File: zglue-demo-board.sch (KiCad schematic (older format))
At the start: 142 parts, among them J1 20021121-00010C4LF, J10 0473460001, J2 DF13A-2P-1.25H, J3 20021121-00010C4LF, J4 2x20_Header_Female, J5 0473460001, J6 556500488, J7 556500488, J8 WE_686115148922, J9 WE_686115148922_FLIPPED, U1 MCP1700T-3302E_TT, U2 NTB0104BQ, U3 NTB0104BQ, U4 NTB0104BQ, U5 93LC56CT-IMC, U6 FT4232HQ, U7 NTB0104BQ, U8 NTB0104BQ, Y1 ASFLMB-12.000MHZ-LC-T

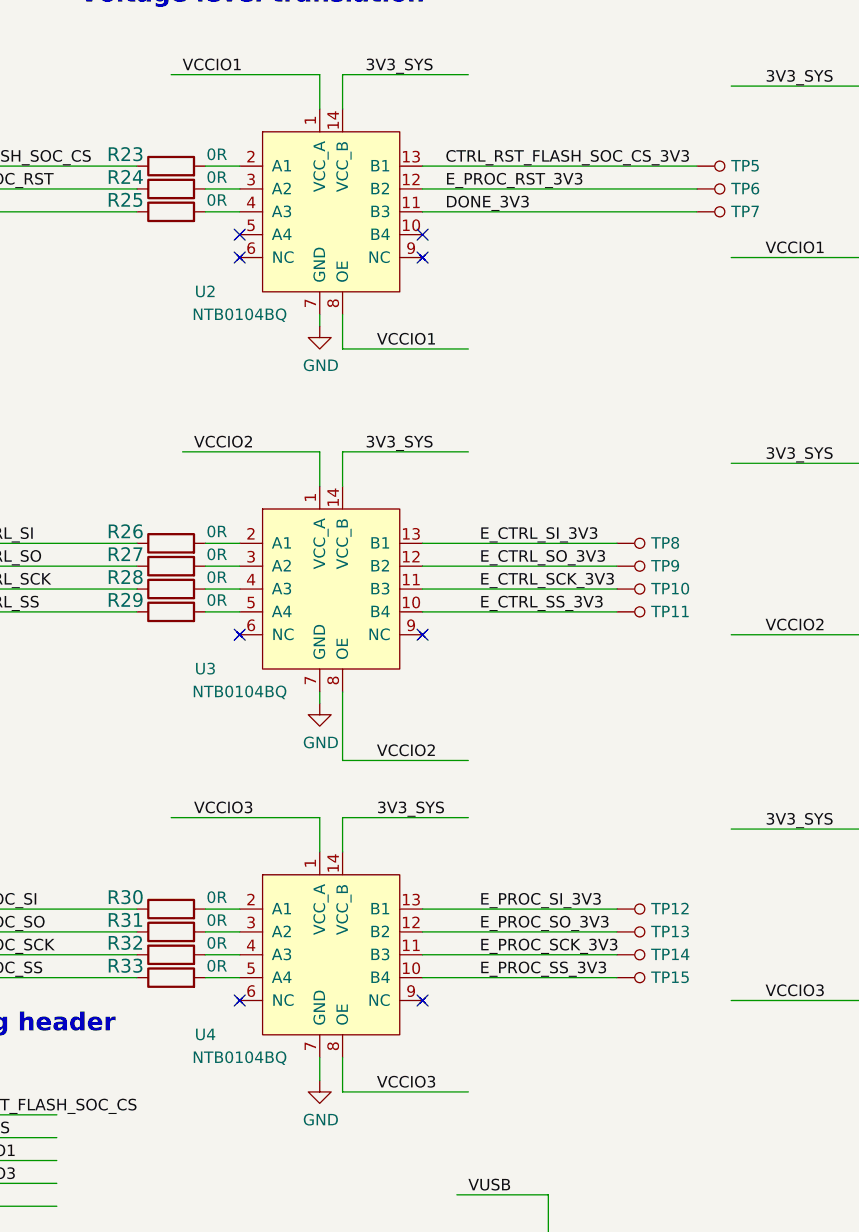
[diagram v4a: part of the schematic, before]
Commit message: Schematic updated after initial bringup
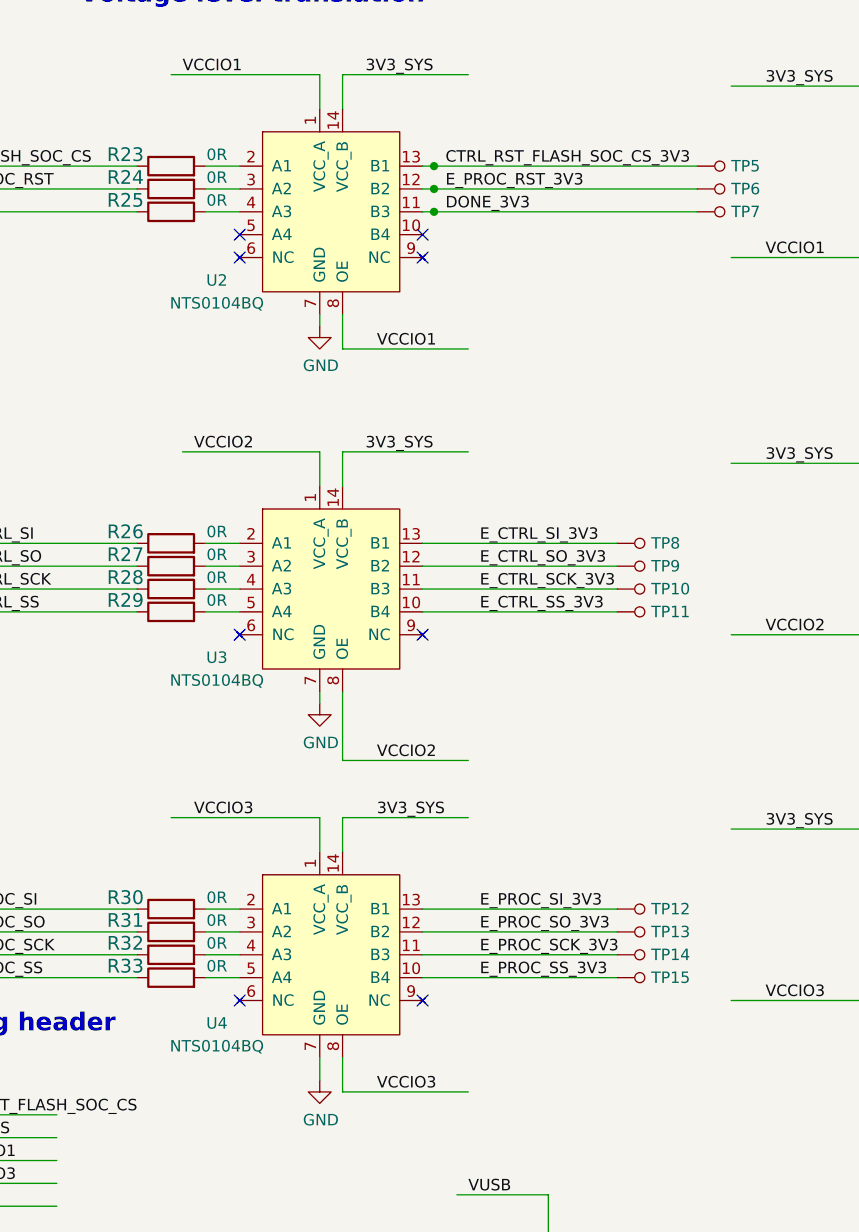
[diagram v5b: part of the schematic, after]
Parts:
- removed U2, U3, U4: NTB0104BQ, antmicro-footprints:QDHVQFN14, symbol antmicroLogicTranslatorsLevelShifters:NTB0104BQ
- added U2, U3, U4: NTS0104BQ, antmicro-footprints:QDHVQFN14, symbol antmicroLogicTranslatorsLevelShifters:NTS0104BQ
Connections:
- wire segments 516 -> 519
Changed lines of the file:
@@
 EESchema Schematic File Version 4
 LIBS:zglue-demo-board-cache
-EELAYER 26 0
+EELAYER 30 0
 EELAYER END
 $Descr A3 16535 11693
@@
 TODO: check pin order\n
 $Comp
-L antmicroLogicTranslatorsLevelShifters:NTB0104BQ U4
-U 1 1 5D99B71D
-P 6800 5000
-F 0 "U4" H 6250 4650 50  0000 C CNN
-F 1 "NTB0104BQ" H 6400 4550 50  0000 C CNN
-F 2 "antmicro-footprints:QDHVQFN14" H 7850 5650 50  0001 C CNN
-F 3 "https://datasheet.octopart.com/NTB0104BQ%2C115-NXP-Semiconductors-datasheet-12519051.pdf" H 7450 5750 50  0001 C CNN
-F 4 "NTB0104BQ" H 6800 5536 50  0001 C CNN "MPN"
-F 5 "NXP Semiconductors" H 6800 5537 50  0001 C CNN "Manufacturer"
-	1    6800 5000
-	1    0    0    -1
-$EndComp
-$Comp
 L power:GND #PWR026
 U 1 1 5D9BD547
@@
 $EndComp
 $Comp
-L antmicroLogicTranslatorsLevelShifters:NTB0104BQ U3
-U 1 1 5DC43970
-P 6800 3400
-F 0 "U3" H 6250 3050 50  0000 C CNN
-F 1 "NTB0104BQ" H 6400 2950 50  0000 C CNN
-F 2 "antmicro-footprints:QDHVQFN14" H 7850 4050 50  0001 C CNN
-F 3 "https://datasheet.octopart.com/NTB0104BQ%2C115-NXP-Semiconductors-datasheet-12519051.pdf" H 7450 4150 50  0001 C CNN
-F 4 "NTB0104BQ" H 6800 3936 50  0001 C CNN "MPN"
-F 5 "NXP Semiconductors" H 6800 3937 50  0001 C CNN "Manufacturer"
-	1    6800 3400
-	1    0    0    -1
-$EndComp
-$Comp
 L power:GND #PWR025
 U 1 1 5DC43977
@@
 E_CTRL_SS_3V3
 $Comp
-L antmicroLogicTranslatorsLevelShifters:NTB0104BQ U2
-U 1 1 5DD333E1
-P 6800 1750
-F 0 "U2" H 6250 1400 50  0000 C CNN
-F 1 "NTB0104BQ" H 6400 1300 50  0000 C CNN
-F 2 "antmicro-footprints:QDHVQFN14" H 7850 2400 50  0001 C CNN
-F 3 "https://datasheet.octopart.com/NTB0104BQ%2C115-NXP-Semiconductors-datasheet-12519051.pdf" H 7450 2500 50  0001 C CNN
-F 4 "NTB0104BQ" H 6800 2286 50  0001 C CNN "MPN"
-F 5 "NXP Semiconductors" H 6800 2287 50  0001 C CNN "Manufacturer"
-	1    6800 1750
-	1    0    0    -1
-$EndComp
-$Comp
 L power:GND #PWR024
 U 1 1 5DD333E8
@@
 	5950 1750 4850 1750
 Wire Wire Line
-	8400 1550 7200 1550
+	8400 1550 7250 1550
 Wire Wire Line
-	8400 1750 7200 1750
+	8400 1750 7250 1750
 $Comp
 L antmicroTestPoints:TP_SMD1MM TP5
@@
 NoConn ~ 7200 5200
 Wire Wire Line
-	8400 1650 7200 1650
+	8400 1650 7250 1650
 Text Label 5150 1650 0    50   ~ 0
 E_PROC_RST
@@
 Wire Wire Line
 	11400 3950 10750 3950
+$Comp
+L antmicroLogicTranslatorsLevelShifters:NTS0104BQ U2
+U 1 1 5DE18FC3
+P 6800 1750
+F 0 "U2" H 6300 1450 50  0000 C CNN
+F 1 "NTS0104BQ" H 6300 1350 50  0000 C CNN
+F 2 "antmicro-footprints:QDHVQFN14" H 7850 2400 50  0001 C CNN
+F 3 "https://datasheet.octopart.com/NTS0104BQ%2C115-NXP-Semiconductors-datasheet-11805065.pdf" H 7450 2500 50  0001 C CNN
+F 4 "NTS0104BQ" H 6800 2289 50  0001 C CNN "MPN"
+F 5 "NXP Semiconductors" H 6800 2290 50  0001 C CNN "Manufacturer"
+	1    6800 1750
+	1    0    0    -1
+$EndComp
+Connection ~ 7250 1750
+Wire Wire Line
+	7250 1750 7200 1750
+Connection ~ 7250 1650
+Wire Wire Line
+	7250 1650 7200 1650
+Connection ~ 7250 1550
+Wire Wire Line
+	7250 1550 7200 1550
+$Comp
+L antmicroLogicTranslatorsLevelShifters:NTS0104BQ U3
+U 1 1 5DE1ADF0
+P 6800 3400
+F 0 "U3" H 6300 3100 50  0000 C CNN
+F 1 "NTS0104BQ" H 6300 3000 50  0000 C CNN
+F 2 "antmicro-footprints:QDHVQFN14" H 7850 4050 50  0001 C CNN
+F 3 "https://datasheet.octopart.com/NTS0104BQ%2C115-NXP-Semiconductors-datasheet-11805065.pdf" H 7450 4150 50  0001 C CNN
+F 4 "NTS0104BQ" H 6800 3939 50  0001 C CNN "MPN"
+F 5 "NXP Semiconductors" H 6800 3940 50  0001 C CNN "Manufacturer"
+	1    6800 3400
+	1    0    0    -1
+$EndComp
+$Comp
+L antmicroLogicTranslatorsLevelShifters:NTS0104BQ U4
+U 1 1 5DE1BA96
+P 6800 5000
+F 0 "U4" H 6300 4700 50  0000 C CNN
+F 1 "NTS0104BQ" H 6300 4600 50  0000 C CNN
+F 2 "antmicro-footprints:QDHVQFN14" H 7850 5650 50  0001 C CNN
+F 3 "https://datasheet.octopart.com/NTS0104BQ%2C115-NXP-Semiconductors-datasheet-11805065.pdf" H 7450 5750 50  0001 C CNN
+F 4 "NTS0104BQ" H 6800 5539 50  0001 C CNN "MPN"
+F 5 "NXP Semiconductors" H 6800 5540 50  0001 C CNN "Manufacturer"
+	1    6800 5000
+	1    0    0    -1
+$EndComp
 $EndSCHEMATC

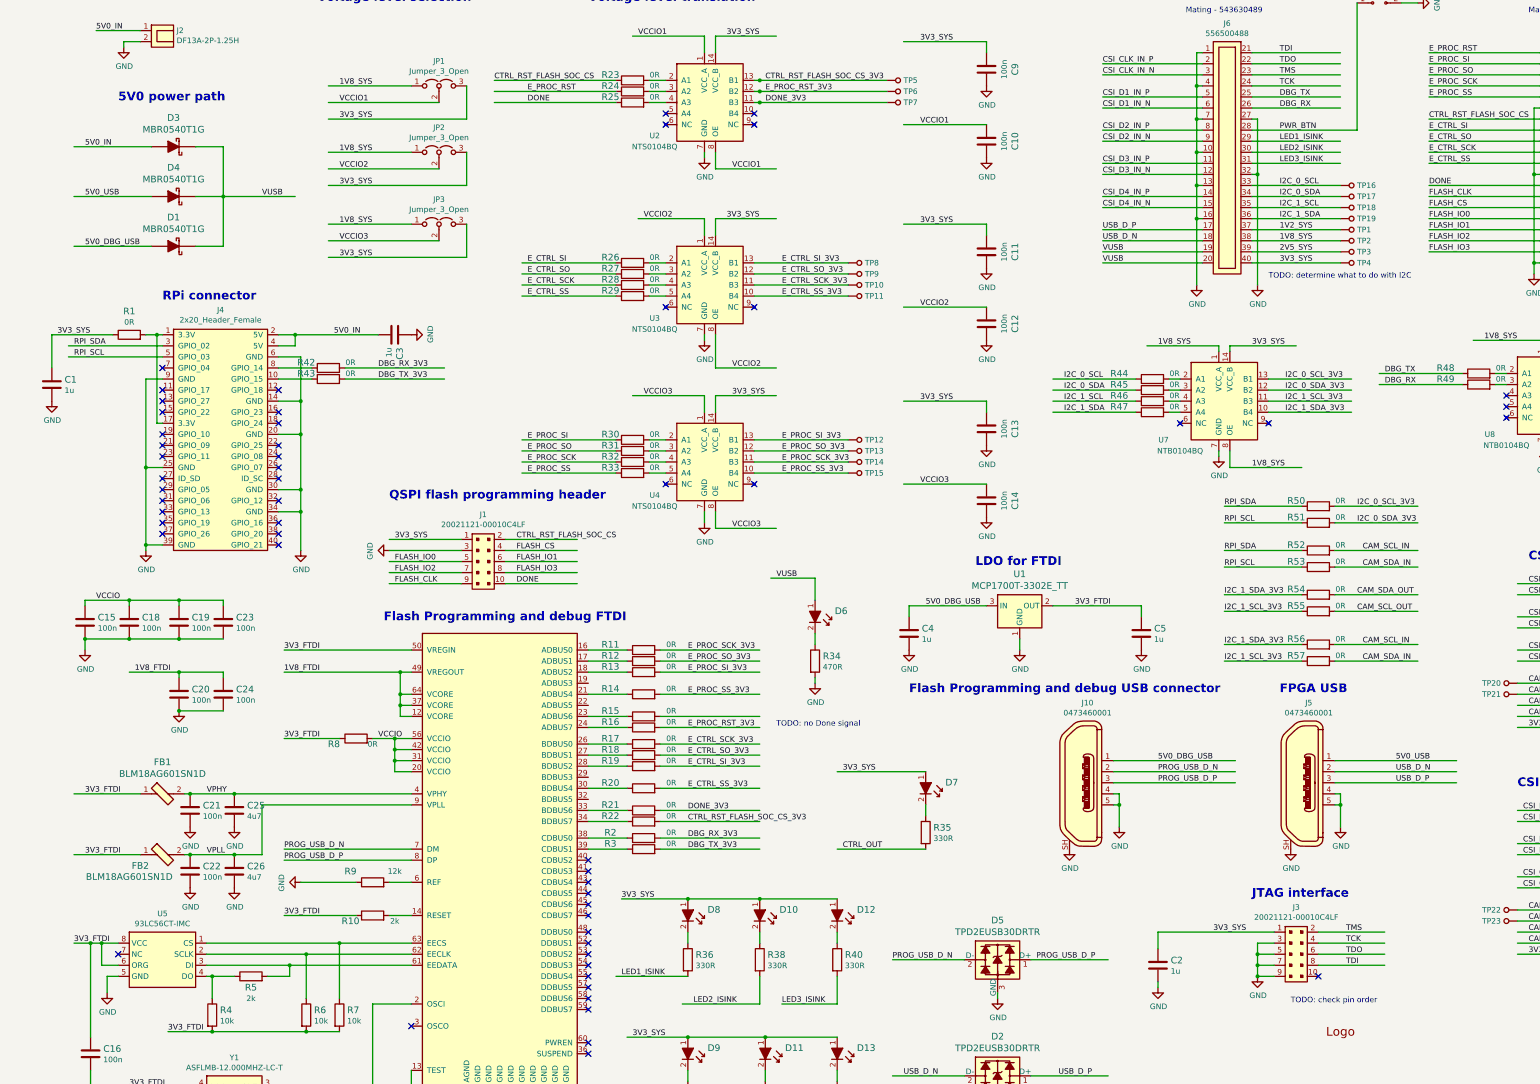
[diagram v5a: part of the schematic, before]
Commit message: Started revision 1.1, moved components to bottom side
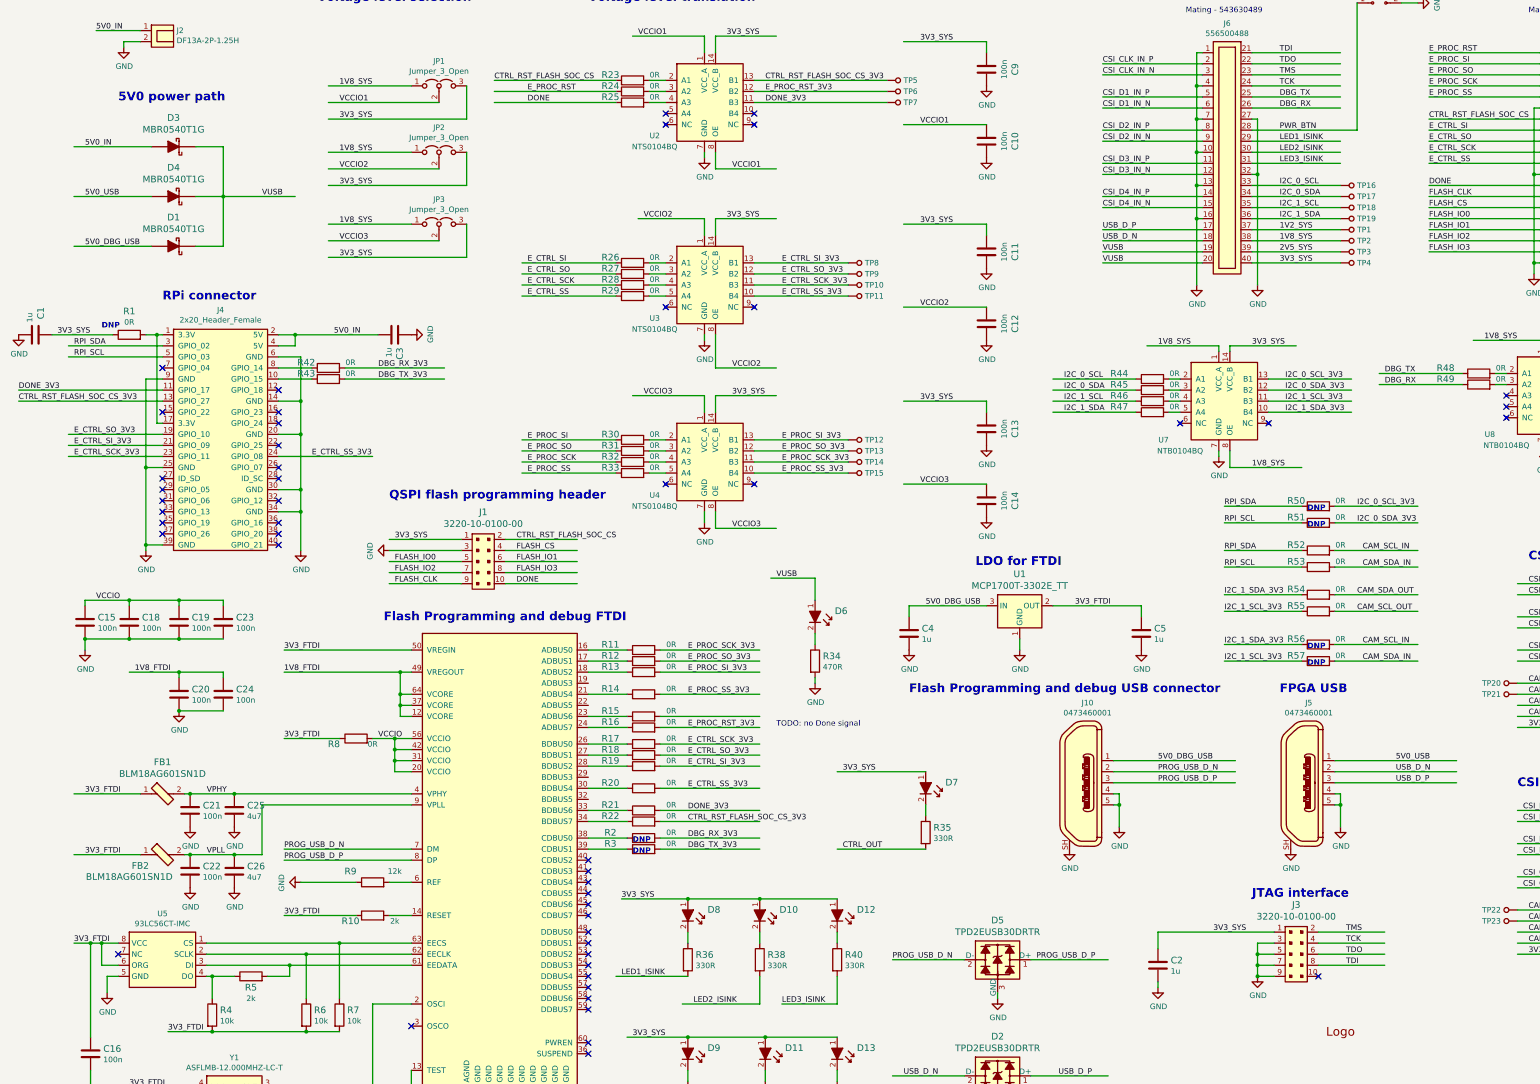
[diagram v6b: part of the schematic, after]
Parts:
- removed J1, J3: 20021121-00010C4LF, antmicro-footprints:PinHeader_2x5_P1.27mm, symbol antmicroRectangularConnectorsHeadersMalePins:20021121-00010C4LF
- added J1, J3: 3220-10-0100-00, antmicro-footprints:PinHeader_2x5_P1.27mm_Drill.7mm, symbol antmicroRectangularConnectorsHeadersMalePins:3220-10-0100-00
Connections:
- wire segments 519 -> 521
- no-connect marks 59 -> 53
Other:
- note added: "DNP"
- note removed: "TODO: check pin order\n"
- note removed: "TODO: determine what to do with I2C"
- moved on the sheet: C1
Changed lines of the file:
@@
 Title "zGlue Demo Board"
 Date ""
-Rev "1.0"
+Rev "1.1"
 Comp "Antmicro"
 Comment1 "www.antmicro.com"
@@
 Wire Wire Line
 	1650 1200 1500 1200
-$Comp
-L antmicroRectangularConnectorsHeadersMalePins:20021121-00010C4LF J3
-U 1 1 5DA5DFAD
-P 12100 9450
-F 0 "J3" H 12100 9875 50  0000 C CNN
-F 1 "20021121-00010C4LF" H 12100 9784 50  0000 C CNN
-F 2 "antmicro-footprints:PinHeader_2x5_P1.27mm" H 12300 9650 60  0001 L CNN
-F 3 "https://cdn.amphenol-icc.com/media/wysiwyg/files/drawing/20021121.pdf" H 12300 9750 60  0001 L CNN
-F 4 "20021121-00010C4LF" H 12300 9950 60  0001 L CNN "MPN"
-F 5 "Amphenol ICC (FCI)" H 12300 10550 60  0001 L CNN "Manufacturer"
-	1    12100 9450
-	1    0    0    -1
-$EndComp
 Wire Wire Line
 	11900 9250 10850 9250
@@
 L antmicroCapacitors0603:C_1u_0603 C1
 U 1 1 5DAD330C
-P 850 4300
-F 0 "C1" H 965 4345 60  0000 L CNN
-F 1 "C_1u_0603" H 850 4150 60  0001 C CNN
-F 2 "antmicro-footprints:0603-cap" H 1050 4500 60  0001 L CNN
-F 3 "" H 850 4300 50  0001 C CNN
-F 4 "WALSIN" H 1050 4700 60  0001 L CNN "Manufacturer"
-F 5 "0603X105K160CT" H 1050 4600 60  0001 L CNN "MPN"
-F 6 "1u" H 965 4247 50  0000 L CNN "Val"
-	1    850  4300
-	1    0    0    -1
+P 700 3850
+F 0 "C1" H 450 3900 60  0000 L CNN
+F 1 "C_1u_0603" H 700 3700 60  0001 C CNN
+F 2 "antmicro-footprints:0603-cap" H 900 4050 60  0001 L CNN
+F 3 "" H 700 3850 50  0001 C CNN
+F 4 "WALSIN" H 900 4250 60  0001 L CNN "Manufacturer"
+F 5 "0603X105K160CT" H 900 4150 60  0001 L CNN "MPN"
+F 6 "1u" H 500 3800 50  0000 L CNN "Val"
+	1    700  3850
+	0    1    1    0
 $EndComp
 $Comp
@@
 	1    0    0    -1
 $EndComp
-Wire Wire Line
-	850  3850 850  4150
 $Comp
 L power:GND #PWR01
 U 1 1 5DAEBF7E
-P 850 4450
-F 0 "#PWR01" H 850 4200 50  0001 C CNN
-F 1 "GND" H 855 4277 50  0000 C CNN
-F 2 "" H 850 4450 50  0001 C CNN
-F 3 "" H 850 4450 50  0001 C CNN
-	1    850  4450
+P 550 3850
+F 0 "#PWR01" H 550 3600 50  0001 C CNN
+F 1 "GND" H 555 3677 50  0000 C CNN
+F 2 "" H 550 3850 50  0001 C CNN
+F 3 "" H 550 3850 50  0001 C CNN
+	1    550  3850
 	1    0    0    -1
 $EndComp
@@
 Text Notes 11100 950  0    50   ~ 0
 Mating - 543630489
-Text Notes 12050 9900 0    50   ~ 0
-TODO: check pin order\n
 $Comp
 L power:GND #PWR026
@@
 Wire Wire Line
 	5950 1750 4850 1750
-Wire Wire Line
-	8400 1550 7250 1550
-Wire Wire Line
-	8400 1750 7250 1750
 $Comp
 L antmicroTestPoints:TP_SMD1MM TP5
@@
 NoConn ~ 6400 5200
 NoConn ~ 7200 5200
-Wire Wire Line
-	8400 1650 7250 1650
 Text Label 5150 1650 0    50   ~ 0
 E_PROC_RST
@@
 Text Label 7300 1750 0    50   ~ 0
 DONE_3V3
-Text Notes 11850 3350 0    50   ~ 0
-TODO: determine what to do with I2C
 $Comp
 L antmicroTestPoints:TP_SMD1MM TP19
@@
 	1    0    0    -1
 $EndComp
-$Comp
-L antmicroRectangularConnectorsHeadersMalePins:20021121-00010C4LF J1
-U 1 1 5DB8DE82
-P 4750 5900
-F 0 "J1" H 4750 6325 50  0000 C CNN
-F 1 "20021121-00010C4LF" H 4750 6234 50  0000 C CNN
-F 2 "antmicro-footprints:PinHeader_2x5_P1.27mm" H 4950 6100 60  0001 L CNN
-F 3 "https://cdn.amphenol-icc.com/media/wysiwyg/files/drawing/20021121.pdf" H 4950 6200 60  0001 L CNN
-F 4 "20021121-00010C4LF" H 4950 6400 60  0001 L CNN "MPN"
-F 5 "Amphenol ICC (FCI)" H 4950 7000 60  0001 L CNN "Manufacturer"
-	1    4750 5900
-	1    0    0    -1
-$EndComp
 Wire Wire Line
 	4550 5700 3900 5700
@@
 NoConn ~ 11050 4650
 NoConn ~ 1850 4150
-NoConn ~ 1850 4350
-NoConn ~ 1850 4450
 NoConn ~ 1850 4550
-NoConn ~ 1850 4750
-NoConn ~ 1850 4850
-NoConn ~ 1850 4950
 NoConn ~ 1850 5150
 NoConn ~ 1850 5250
@@
 NoConn ~ 2900 5150
 NoConn ~ 2900 5050
-NoConn ~ 2900 4950
 NoConn ~ 2900 4850
 NoConn ~ 2900 4650
@@
 	1    0    0    -1
 $EndComp
-Connection ~ 7250 1750
-Wire Wire Line
-	7250 1750 7200 1750
-Connection ~ 7250 1650
-Wire Wire Line
-	7250 1650 7200 1650
-Connection ~ 7250 1550
-Wire Wire Line
-	7250 1550 7200 1550
 $Comp
 L antmicroLogicTranslatorsLevelShifters:NTS0104BQ U3
@@
 	1    0    0    -1
 $EndComp
+Wire Wire Line
+	7200 1550 8400 1550
+Wire Wire Line
+	7200 1750 8400 1750
+Wire Wire Line
+	7200 1650 8400 1650
+Text Notes 6100 8450 0    50   ~ 10
+DNP
+Text Notes 6100 8550 0    50   ~ 10
+DNP
+Text Notes 12200 5450 0    50   ~ 10
+DNP
+Text Notes 12200 5600 0    50   ~ 10
+DNP
+Text Notes 12200 6700 0    50   ~ 10
+DNP
+Text Notes 12200 6850 0    50   ~ 10
+DNP
+Text Notes 1300 3800 0    50   ~ 10
+DNP
+Wire Wire Line
+	1850 4450 550  4450
+Wire Wire Line
+	3750 4950 2900 4950
+Wire Wire Line
+	1850 4750 1000 4750
+Wire Wire Line
+	1850 4850 1000 4850
+Wire Wire Line
+	1850 4950 1000 4950
+Wire Wire Line
+	1850 4350 550  4350
+Text Label 550  4350 0    50   ~ 0
+DONE_3V3
+Text Label 1050 4950 0    50   ~ 0
+E_CTRL_SCK_3V3
+Text Label 1050 4750 0    50   ~ 0
+E_CTRL_SO_3V3
+Text Label 1050 4850 0    50   ~ 0
+E_CTRL_SI_3V3
+Text Label 3200 4950 0    50   ~ 0
+E_CTRL_SS_3V3
+Text Label 550  4450 0    50   ~ 0
+CTRL_RST_FLASH_SOC_CS_3V3
+$Comp
+L antmicroRectangularConnectorsHeadersMalePins:3220-10-0100-00 J1
+U 1 1 5E6FE883
+P 4750 5900
+F 0 "J1" H 4750 6347 60  0000 C CNN
+F 1 "3220-10-0100-00" H 4750 6241 60  0000 C CNN
+F 2 "antmicro-footprints:PinHeader_2x5_P1.27mm_Drill.7mm" H 4950 6100 60  0001 L CNN
+F 3 "http://cnctech.us/pdfs/3220-XX-0100-00.pdf" V 4950 6200 60  0001 L CNN
+F 4 "3220-10-0100-00" H 4950 6400 60  0001 L CNN "MPN"
+F 5 "CNC Tech" H 4950 7000 60  0001 L CNN "Manufacturer"
+	1    4750 5900
+	1    0    0    -1
+$EndComp
+$Comp
+L antmicroRectangularConnectorsHeadersMalePins:3220-10-0100-00 J3
+U 1 1 5E70BB15
+P 12100 9450
+F 0 "J3" H 12100 9897 60  0000 C CNN
+F 1 "3220-10-0100-00" H 12100 9791 60  0000 C CNN
+F 2 "antmicro-footprints:PinHeader_2x5_P1.27mm_Drill.7mm" H 12300 9650 60  0001 L CNN
+F 3 "http://cnctech.us/pdfs/3220-XX-0100-00.pdf" V 12300 9750 60  0001 L CNN
+F 4 "3220-10-0100-00" H 12300 9950 60  0001 L CNN "MPN"
+F 5 "CNC Tech" H 12300 10550 60  0001 L CNN "Manufacturer"
+	1    12100 9450
+	1    0    0    -1
+$EndComp
